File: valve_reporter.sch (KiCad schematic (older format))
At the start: 57 parts, among them J1 Screw_Terminal_01x05, J2 Screw_Terminal_01x14, K1 G5LE-1, Q1 2N3904, U1 NodeMCU_1.0_(ESP-12E), U2 MC7805CTG

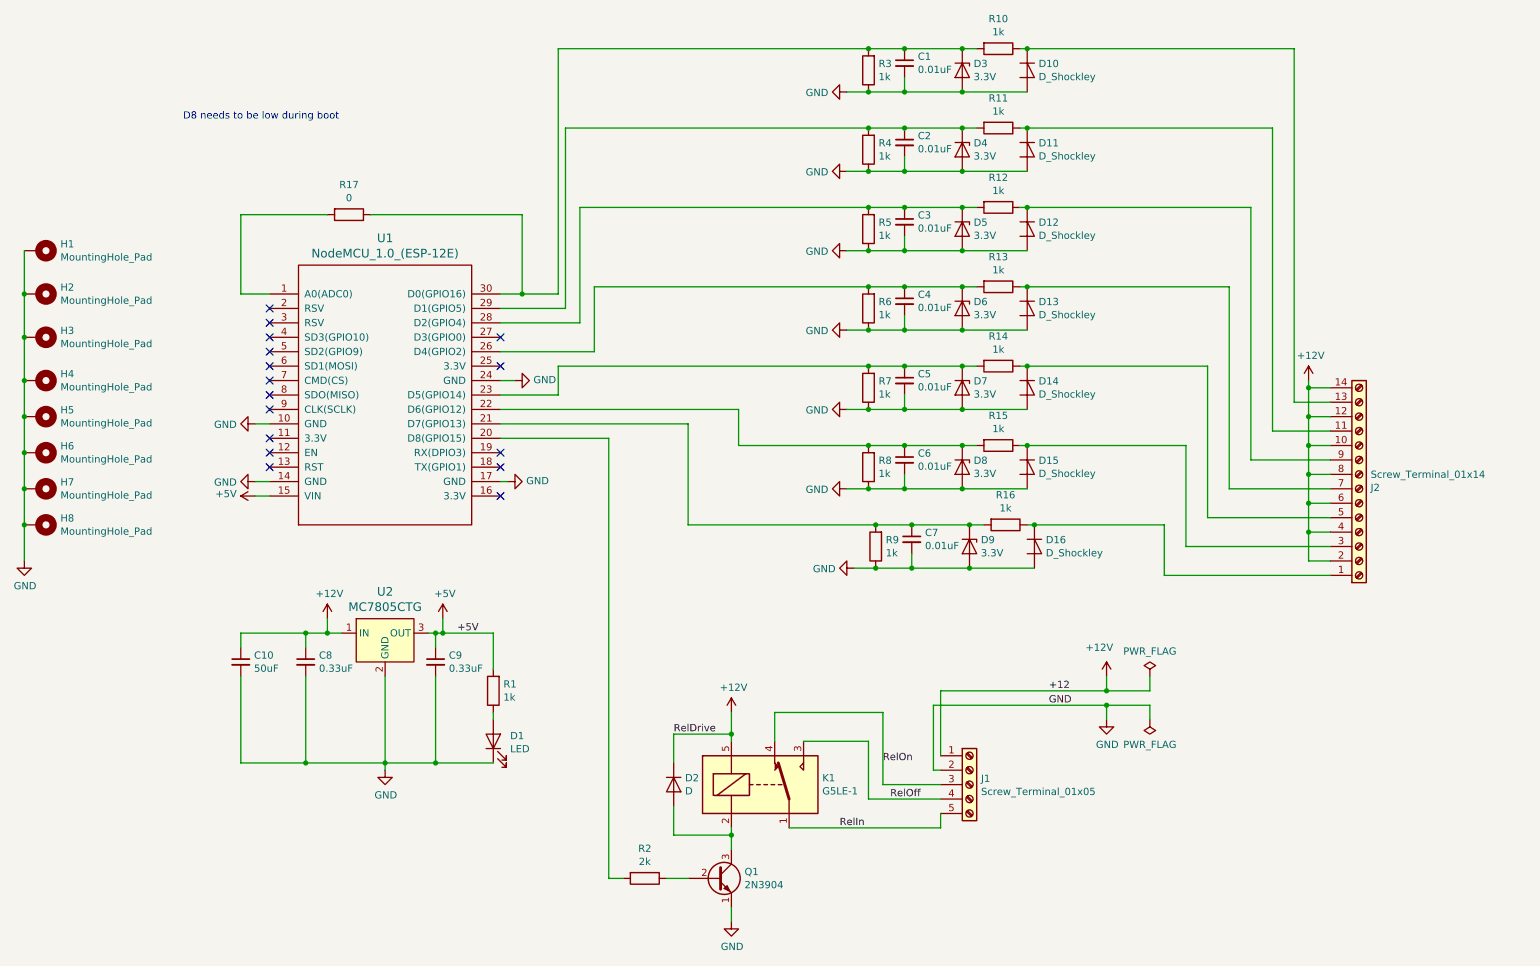
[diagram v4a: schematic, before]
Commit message: Use mosfet to drive relay add test points
todo:
- connect test points
- SMD relay?...
- check holes sizes
- 12V power plane
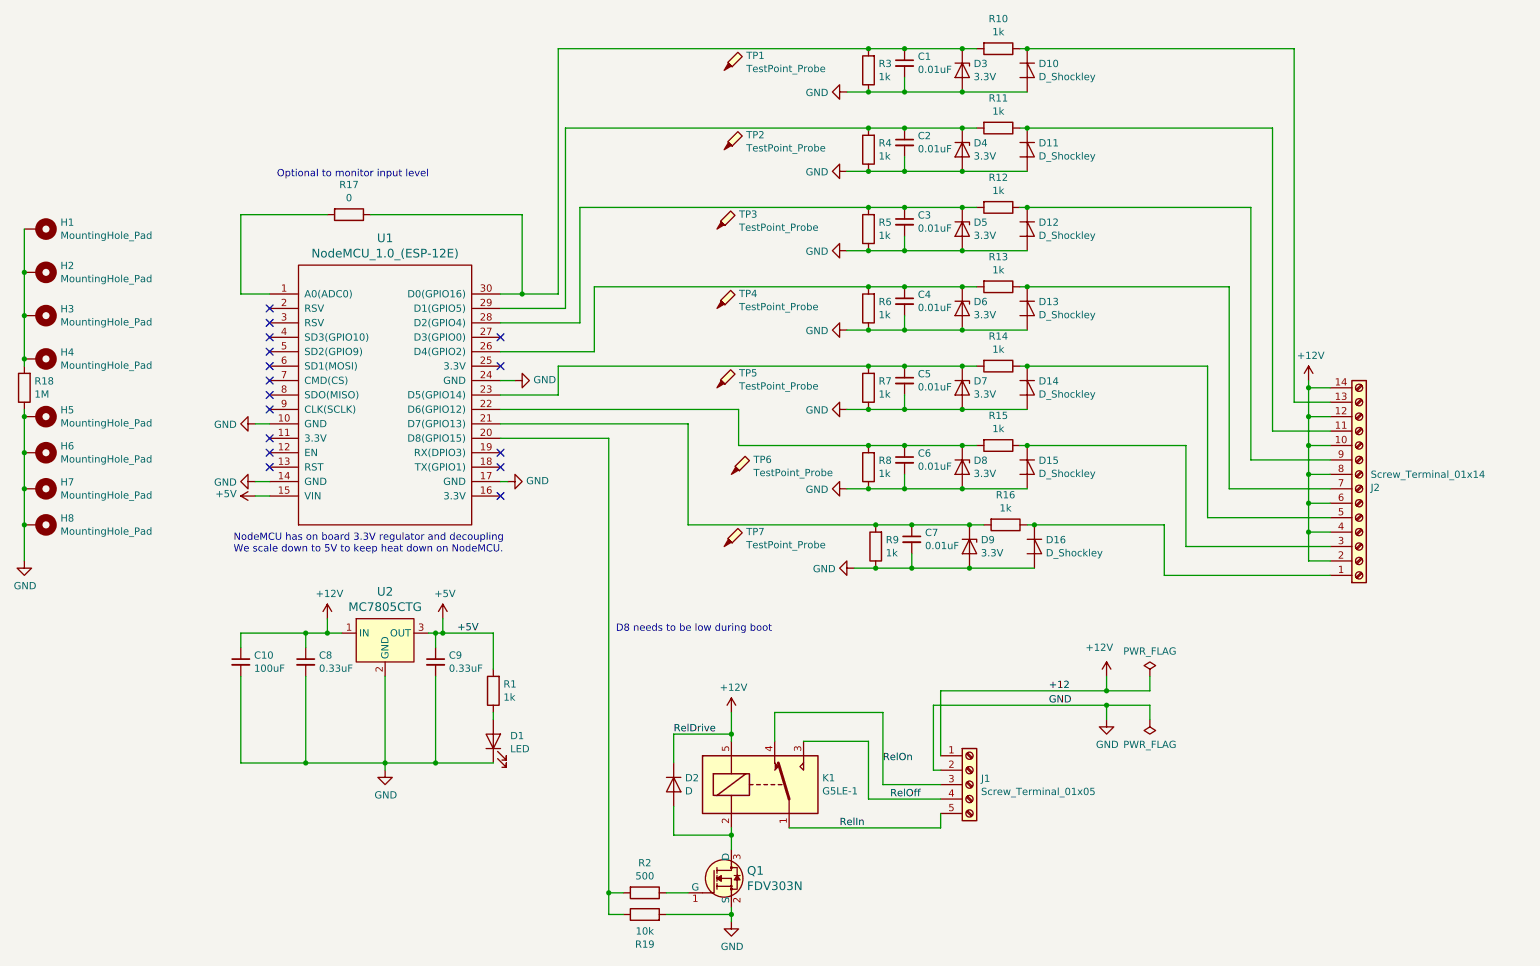
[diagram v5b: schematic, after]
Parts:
- removed Q1: 2N3904, Package_TO_SOT_THT:TO-92_Inline, symbol Transistor_BJT:2N3904
- added Q1: FDV303N, digikey-footprints:SOT-23-3, symbol dk_Transistors-FETs-MOSFETs-Single:FDV303N
- added R18: 1M, Resistor_SMD:R_1206_3216Metric_Pad1.42x1.75mm_HandSolder, symbol Device:R
- added R19: 10k, Resistor_SMD:R_1206_3216Metric_Pad1.42x1.75mm_HandSolder, symbol Device:R
- added TP1, TP2, TP3, TP4, TP5, TP6, TP7: TestPoint_Probe, symbol Connector:TestPoint_Probe
- C10: value 50uF -> 100uF
- R2: value 2k -> 500
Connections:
- net GND: now also Q1.2 (S), R18.1, R19.2; no longer H1.1, H2.1, H3.1, H4.1
- net at R2.2, U1.20 (D8(GPIO15)): now also R19.1
- net at D2.2 (A), K1.2: now also Q1.3 (D)
- net at R2.1: now also Q1.1 (G)
- new net: H1.1, H2.1, H3.1, H4.1, R18.2
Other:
- note added: "NodeMCU has on board 3.3V regulator and decoupling\nWe scale down to 5V to keep heat down on NodeMCU."
- note added: "Optional to monitor input level"
- moved on the sheet: H1, H2, H3, H4, R2
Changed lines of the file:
@@
 Wire Wire Line
 	3400 5200 3400 5800
-Text Notes 2000 1350 0    50   ~ 0
+Text Notes 5000 4900 0    50   ~ 0
 D8 needs to be low during boot
 $Comp
@@
 $EndComp
 $Comp
-L Transistor_BJT:2N3904 Q1
-U 1 1 5C568BC6
-P 5700 6600
-F 0 "Q1" H 5891 6646 50  0000 L CNN
-F 1 "2N3904" H 5891 6555 50  0000 L CNN
-F 2 "Package_TO_SOT_THT:TO-92_Inline" H 5900 6525 50  0001 L CIN
-F 3 "https://www.fairchildsemi.com/datasheets/2N/2N3904.pdf" H 5700 6600 50  0001 L CNN
-	1    5700 6600
-	1    0    0    -1
-$EndComp
-$Comp
 L Device:D D2
 U 1 1 5C568C95
@@
 L Device:R R2
 U 1 1 5C569AE5
-P 5200 6600
-F 0 "R2" V 4993 6600 50  0000 C CNN
-F 1 "2k" V 5084 6600 50  0000 C CNN
-F 2 "Resistor_SMD:R_1206_3216Metric_Pad1.42x1.75mm_HandSolder" V 5130 6600 50  0001 C CNN
-F 3 "~" H 5200 6600 50  0001 C CNN
-	1    5200 6600
+P 5200 6700
+F 0 "R2" V 4993 6700 50  0000 C CNN
+F 1 "500" V 5084 6700 50  0000 C CNN
+F 2 "Resistor_SMD:R_1206_3216Metric_Pad1.42x1.75mm_HandSolder" V 5130 6700 50  0001 C CNN
+F 3 "~" H 5200 6700 50  0001 C CNN
+	1    5200 6700
 	0    1    1    0
 $EndComp
@@
 Wire Wire Line
 	5800 6300 5800 6250
-Wire Wire Line
-	5350 6600 5500 6600
 $Comp
 L power:GND #PWR0113
@@
 $EndComp
 Wire Wire Line
-	5800 6900 5800 6800
-Wire Wire Line
-	4950 6600 5050 6600
+	5800 6900 5800 6850
 Wire Wire Line
 	6100 5650 6100 5450
@@
 	6750 1150 6600 1150
 Connection ~ 6750 1150
-Wire Wire Line
-	4950 6600 4950 3550
 Wire Wire Line
 	4950 3550 4200 3550
@@
 L Mechanical:MountingHole_Pad H1
 U 1 1 5C7A6D18
-P 1000 2250
-F 0 "H1" V 954 2400 50  0000 L CNN
-F 1 "MountingHole_Pad" V 1045 2400 50  0000 L CNN
-F 2 "MountingHole:MountingHole_3.2mm_M3_ISO7380_Pad" H 1000 2250 50  0001 C CNN
-F 3 "~" H 1000 2250 50  0001 C CNN
-	1    1000 2250
+P 1000 2100
+F 0 "H1" V 954 2250 50  0000 L CNN
+F 1 "MountingHole_Pad" V 1045 2250 50  0000 L CNN
+F 2 "MountingHole:MountingHole_3.2mm_M3_ISO7380_Pad" H 1000 2100 50  0001 C CNN
+F 3 "~" H 1000 2100 50  0001 C CNN
+	1    1000 2100
 	0    1    1    0
 $EndComp
@@
 L Mechanical:MountingHole_Pad H2
 U 1 1 5C7A6DAA
-P 1000 2550
-F 0 "H2" V 954 2700 50  0000 L CNN
-F 1 "MountingHole_Pad" V 1045 2700 50  0000 L CNN
-F 2 "MountingHole:MountingHole_3.2mm_M3_ISO7380_Pad" H 1000 2550 50  0001 C CNN
-F 3 "~" H 1000 2550 50  0001 C CNN
-	1    1000 2550
+P 1000 2400
+F 0 "H2" V 954 2550 50  0000 L CNN
+F 1 "MountingHole_Pad" V 1045 2550 50  0000 L CNN
+F 2 "MountingHole:MountingHole_3.2mm_M3_ISO7380_Pad" H 1000 2400 50  0001 C CNN
+F 3 "~" H 1000 2400 50  0001 C CNN
+	1    1000 2400
 	0    1    1    0
 $EndComp
@@
 L Mechanical:MountingHole_Pad H3
 U 1 1 5C7A6E22
-P 1000 2850
-F 0 "H3" V 954 3000 50  0000 L CNN
-F 1 "MountingHole_Pad" V 1045 3000 50  0000 L CNN
-F 2 "MountingHole:MountingHole_3.2mm_M3_ISO7380_Pad" H 1000 2850 50  0001 C CNN
-F 3 "~" H 1000 2850 50  0001 C CNN
-	1    1000 2850
+P 1000 2700
+F 0 "H3" V 954 2850 50  0000 L CNN
+F 1 "MountingHole_Pad" V 1045 2850 50  0000 L CNN
+F 2 "MountingHole:MountingHole_3.2mm_M3_ISO7380_Pad" H 1000 2700 50  0001 C CNN
+F 3 "~" H 1000 2700 50  0001 C CNN
+	1    1000 2700
 	0    1    1    0
 $EndComp
@@
 L Mechanical:MountingHole_Pad H4
 U 1 1 5C7A6E9E
-P 1000 3150
-F 0 "H4" V 954 3300 50  0000 L CNN
-F 1 "MountingHole_Pad" V 1045 3300 50  0000 L CNN
-F 2 "MountingHole:MountingHole_3.2mm_M3_ISO7380_Pad" H 1000 3150 50  0001 C CNN
-F 3 "~" H 1000 3150 50  0001 C CNN
-	1    1000 3150
-	0    1    1    0
-$EndComp
-Wire Wire Line
-	900  3150 900  2850
-Wire Wire Line
-	900  2850 900  2550
-Connection ~ 900  2850
-Wire Wire Line
-	900  2550 900  2250
-Connection ~ 900  2550
+P 1000 3000
+F 0 "H4" V 954 3150 50  0000 L CNN
+F 1 "MountingHole_Pad" V 1045 3150 50  0000 L CNN
+F 2 "MountingHole:MountingHole_3.2mm_M3_ISO7380_Pad" H 1000 3000 50  0001 C CNN
+F 3 "~" H 1000 3000 50  0001 C CNN
+	1    1000 3000
+	0    1    1    0
+$EndComp
 $Comp
 L power:GND #PWR0105
@@
 Wire Wire Line
 	900  4400 900  4150
-Connection ~ 900  3150
 $Comp
 L Connector:Screw_Terminal_01x05 J1
@@
 	0    1    1    0
 $EndComp
-Connection ~ 900  3400
-Wire Wire Line
-	900  3400 900  3150
 Connection ~ 900  3650
 Wire Wire Line
@@
 P 2400 5100
 F 0 "C10" H 2492 5146 50  0000 L CNN
-F 1 "50uF" H 2492 5055 50  0000 L CNN
+F 1 "100uF" H 2492 5055 50  0000 L CNN
 F 2 "Capacitor_SMD:C_2816_7142Metric_Pad3.20x4.45mm_HandSolder" H 2400 5100 50  0001 C CNN
 F 3 "~" H 2400 5100 50  0001 C CNN
@@
 	2400 5800 2850 5800
 Connection ~ 2850 5800
+Text Notes 2650 1750 0    50   ~ 0
+Optional to monitor input level
+Text Notes 2350 4350 0    50   ~ 0
+NodeMCU has on board 3.3V regulator and decoupling\nWe scale down to 5V to keep heat down on NodeMCU.
+$Comp
+L dk_Transistors-FETs-MOSFETs-Single:FDV303N Q1
+U 1 1 5C553D13
+P 5800 6600
+F 0 "Q1" H 5908 6653 60  0000 L CNN
+F 1 "FDV303N" H 5908 6547 60  0000 L CNN
+F 2 "digikey-footprints:SOT-23-3" H 6000 6800 60  0001 L CNN
+F 3 "https://media.digikey.com/pdf/Data%20Sheets/Fairchild%20PDFs/FDV303N.pdf" H 6000 6900 60  0001 L CNN
+F 4 "FDV303NCT-ND" H 6000 7000 60  0001 L CNN "Digi-Key_PN"
+F 5 "FDV303N" H 6000 7100 60  0001 L CNN "MPN"
+F 6 "Discrete Semiconductor Products" H 6000 7200 60  0001 L CNN "Category"
+F 7 "Transistors - FETs, MOSFETs - Single" H 6000 7300 60  0001 L CNN "Family"
+F 8 "https://media.digikey.com/pdf/Data%20Sheets/Fairchild%20PDFs/FDV303N.pdf" H 6000 7400 60  0001 L CNN "DK_Datasheet_Link"
+F 9 "/product-detail/en/on-semiconductor/FDV303N/FDV303NCT-ND/458956" H 6000 7500 60  0001 L CNN "DK_Detail_Page"
+F 10 "MOSFET N-CH 25V 680MA SOT-23" H 6000 7600 60  0001 L CNN "Description"
+F 11 "ON Semiconductor" H 6000 7700 60  0001 L CNN "Manufacturer"
+F 12 "Active" H 6000 7800 60  0001 L CNN "Status"
+	1    5800 6600
+	1    0    0    -1
+$EndComp
+Wire Wire Line
+	5350 6700 5500 6700
+Wire Wire Line
+	4950 6700 5050 6700
+Wire Wire Line
+	4950 3550 4950 6700
+$Comp
+L Device:R R19
+U 1 1 5C574FF1
+P 5200 6850
+F 0 "R19" V 4993 6850 50  0000 C CNN
+F 1 "10k" V 5084 6850 50  0000 C CNN
+F 2 "Resistor_SMD:R_1206_3216Metric_Pad1.42x1.75mm_HandSolder" V 5130 6850 50  0001 C CNN
+F 3 "~" H 5200 6850 50  0001 C CNN
+	1    5200 6850
+	0    -1   -1   0
+$EndComp
+Wire Wire Line
+	4950 6700 4950 6850
+Wire Wire Line
+	4950 6850 5050 6850
+Connection ~ 4950 6700
+Wire Wire Line
+	5350 6850 5800 6850
+Connection ~ 5800 6850
+Wire Wire Line
+	5800 6850 5800 6800
+$Comp
+L Device:R R18
+U 1 1 5C5A3068
+P 900 3200
+F 0 "R18" H 830 3154 50  0000 R CNN
+F 1 "1M" H 830 3245 50  0000 R CNN
+F 2 "Resistor_SMD:R_1206_3216Metric_Pad1.42x1.75mm_HandSolder" V 830 3200 50  0001 C CNN
+F 3 "~" H 900 3200 50  0001 C CNN
+	1    900  3200
+	-1   0    0    1
+$EndComp
+Wire Wire Line
+	900  3350 900  3400
+Connection ~ 900  3400
+Wire Wire Line
+	900  3050 900  3000
+Wire Wire Line
+	900  3000 900  2700
+Connection ~ 900  3000
+Wire Wire Line
+	900  2700 900  2400
+Connection ~ 900  2700
+Wire Wire Line
+	900  2400 900  2100
+Connection ~ 900  2400
+$Comp
+L Connector:TestPoint_Probe TP1
+U 1 1 5C5DE5A9
+P 5750 1000
+F 0 "TP1" H 5903 1102 50  0000 L CNN
+F 1 "TestPoint_Probe" H 5903 1011 50  0000 L CNN
+F 2 "" H 5950 1000 50  0001 C CNN
+F 3 "~" H 5950 1000 50  0001 C CNN
+	1    5750 1000
+	1    0    0    -1
+$EndComp
+$Comp
+L Connector:TestPoint_Probe TP2
+U 1 1 5C5DE6F3
+P 5750 1550
+F 0 "TP2" H 5903 1652 50  0000 L CNN
+F 1 "TestPoint_Probe" H 5903 1561 50  0000 L CNN
+F 2 "" H 5950 1550 50  0001 C CNN
+F 3 "~" H 5950 1550 50  0001 C CNN
+	1    5750 1550
+	1    0    0    -1
+$EndComp
+$Comp
+L Connector:TestPoint_Probe TP3
+U 1 1 5C5DE797
+P 5700 2100
+F 0 "TP3" H 5853 2202 50  0000 L CNN
+F 1 "TestPoint_Probe" H 5853 2111 50  0000 L CNN
+F 2 "" H 5900 2100 50  0001 C CNN
+F 3 "~" H 5900 2100 50  0001 C CNN
+	1    5700 2100
+	1    0    0    -1
+$EndComp
+$Comp
+L Connector:TestPoint_Probe TP4
+U 1 1 5C5DE849
+P 5700 2650
+F 0 "TP4" H 5853 2752 50  0000 L CNN
+F 1 "TestPoint_Probe" H 5853 2661 50  0000 L CNN
+F 2 "" H 5900 2650 50  0001 C CNN
+F 3 "~" H 5900 2650 50  0001 C CNN
+	1    5700 2650
+	1    0    0    -1
+$EndComp
+$Comp
+L Connector:TestPoint_Probe TP5
+U 1 1 5C5DE8E9
+P 5700 3200
+F 0 "TP5" H 5853 3302 50  0000 L CNN
+F 1 "TestPoint_Probe" H 5853 3211 50  0000 L CNN
+F 2 "" H 5900 3200 50  0001 C CNN
+F 3 "~" H 5900 3200 50  0001 C CNN
+	1    5700 3200
+	1    0    0    -1
+$EndComp
+$Comp
+L Connector:TestPoint_Probe TP6
+U 1 1 5C5DE98F
+P 5800 3800
+F 0 "TP6" H 5953 3902 50  0000 L CNN
+F 1 "TestPoint_Probe" H 5953 3811 50  0000 L CNN
+F 2 "" H 6000 3800 50  0001 C CNN
+F 3 "~" H 6000 3800 50  0001 C CNN
+	1    5800 3800
+	1    0    0    -1
+$EndComp
+$Comp
+L Connector:TestPoint_Probe TP7
+U 1 1 5C5DEA37
+P 5750 4300
+F 0 "TP7" H 5903 4402 50  0000 L CNN
+F 1 "TestPoint_Probe" H 5903 4311 50  0000 L CNN
+F 2 "" H 5950 4300 50  0001 C CNN
+F 3 "~" H 5950 4300 50  0001 C CNN
+	1    5750 4300
+	1    0    0    -1
+$EndComp
 $EndSCHEMATC
